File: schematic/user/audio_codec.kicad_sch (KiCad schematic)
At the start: 27 parts, among them U4 TLV320AIC3254IRHBR

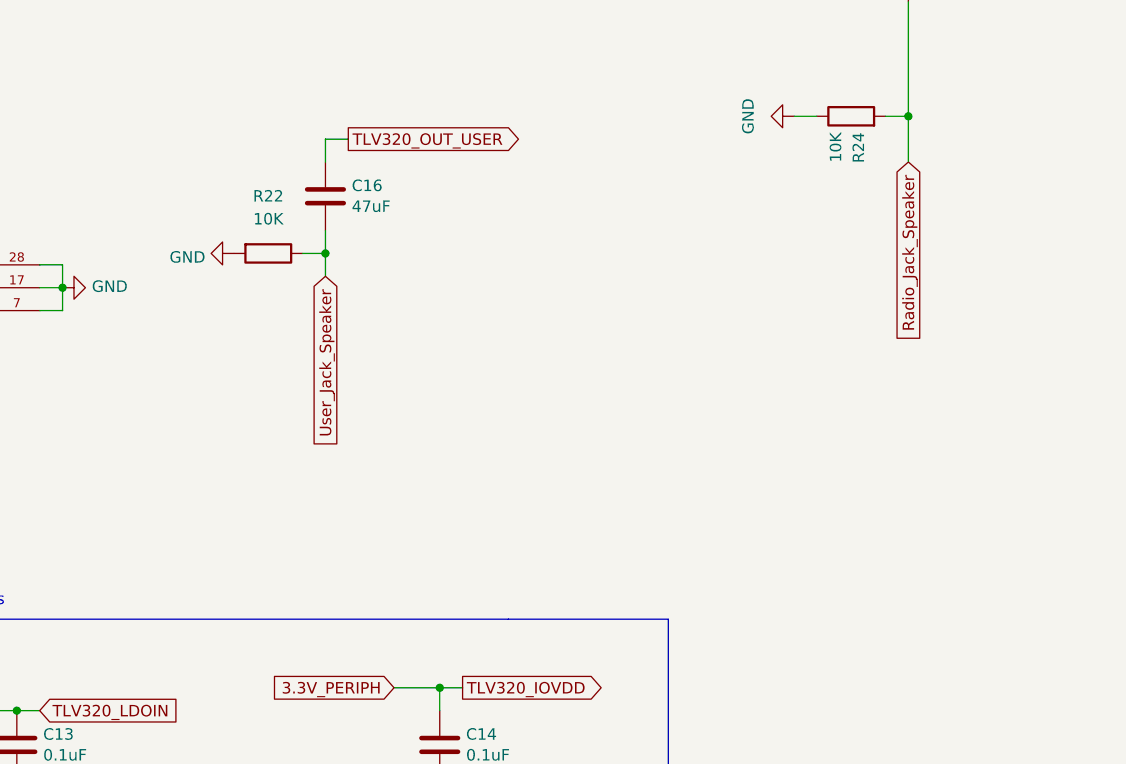
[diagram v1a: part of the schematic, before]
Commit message: v0.7 board: re-add output LPF for audio jacks.
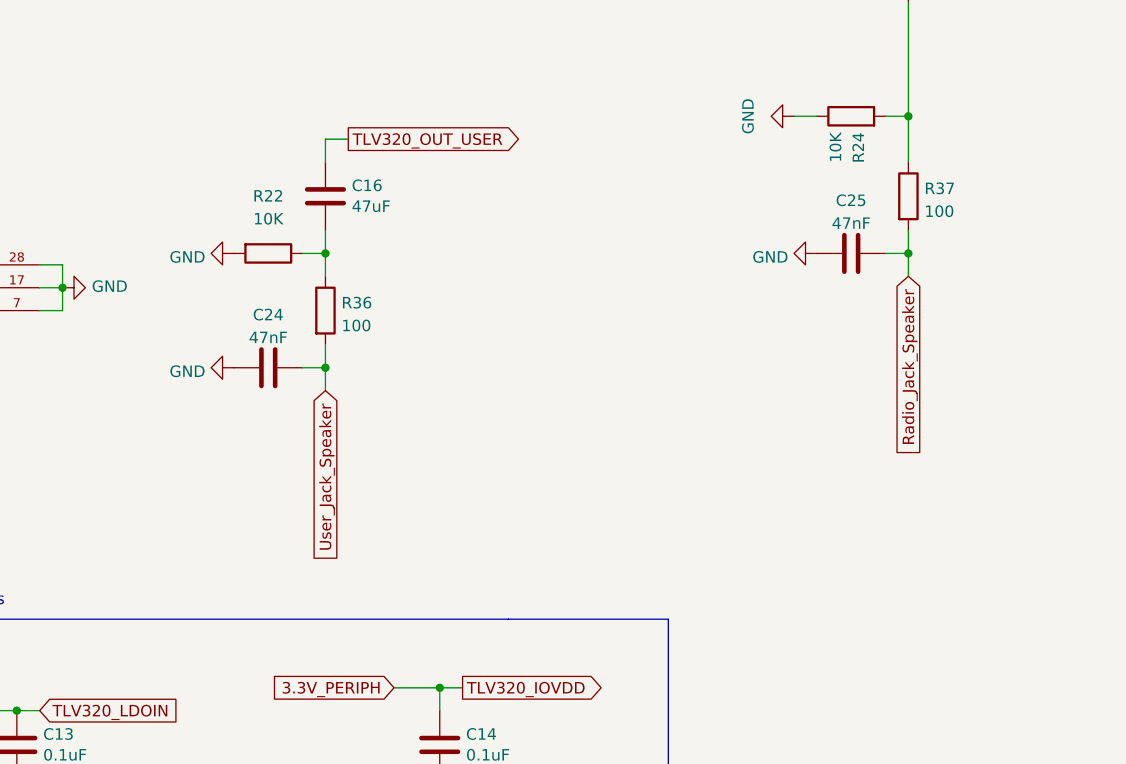
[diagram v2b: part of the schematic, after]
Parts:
- added C24, C25: 47nF, Capacitor_SMD:C_0402_1005Metric, symbol Device:C
- added R36, R37: 100, Resistor_SMD:R_0402_1005Metric, symbol Device:R
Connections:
- net GND: now also C24.1, C25.1
- net Radio_Jack_Speaker: now also C25.2, R37.2; no longer C17.2, R24.2
- net User_Jack_Speaker: now also C24.2, R36.2; no longer C16.2, R22.1
- new net: C16.2, R22.1, R36.1
- new net: C17.2, R24.2, R37.1
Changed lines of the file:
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@@
   (junction (at 39.37 177.8) (diameter 0) (color 0 0 0 0)
   )
+  (junction (at 200.66 123.19) (diameter 0) (color 0 0 0 0)
+  )
   (junction (at 200.66 107.95) (diameter 0) (color 0 0 0 0)
   )
@@
   )
   (junction (at 255.27 27.94) (diameter 0) (color 0 0 0 0)
+  )
+  (junction (at 135.89 135.89) (diameter 0) (color 0 0 0 0)
   )
   (junction (at 106.68 127) (diameter 0) (color 0 0 0 0)
@@
     (stroke (width 0) (type default) (color 0 0 0 0))
   )
+  (wire (pts (xy 200.66 123.19) (xy 200.66 125.73))
+    (stroke (width 0) (type default) (color 0 0 0 0))
+  )
   (wire (pts (xy 106.68 129.54) (xy 106.68 127))
     (stroke (width 0) (type default) (color 0 0 0 0))
@@
     (stroke (width 0) (type default) (color 0 0 0 0))
   )
+  (wire (pts (xy 198.12 123.19) (xy 200.66 123.19))
+    (stroke (width 0) (type default) (color 0 0 0 0))
+  )
   (wire (pts (xy 53.34 83.82) (xy 49.53 83.82))
     (stroke (width 0) (type default) (color 0 0 0 0))
@@
     (stroke (width 0) (type default) (color 0 0 0 0))
   )
+  (wire (pts (xy 133.35 135.89) (xy 135.89 135.89))
+    (stroke (width 0) (type default) (color 0 0 0 0))
+  )
   (wire (pts (xy 40.64 177.8) (xy 39.37 177.8))
     (stroke (width 0) (type default) (color 0 0 0 0))
@@
     (stroke (width 0) (type default) (color 0 0 0 0))
   )
+  (wire (pts (xy 200.66 120.65) (xy 200.66 123.19))
+    (stroke (width 0) (type default) (color 0 0 0 0))
+  )
   (wire (pts (xy 160.02 68.58) (xy 161.29 68.58))
     (stroke (width 0) (type default) (color 0 0 0 0))
@@
     (stroke (width 0) (type default) (color 0 0 0 0))
   )
+  (wire (pts (xy 135.89 135.89) (xy 135.89 133.35))
+    (stroke (width 0) (type default) (color 0 0 0 0))
+  )
   (wire (pts (xy 53.34 88.9) (xy 49.53 88.9))
     (stroke (width 0) (type default) (color 0 0 0 0))
@@
   )
   (wire (pts (xy 53.34 104.14) (xy 50.8 104.14))
+    (stroke (width 0) (type default) (color 0 0 0 0))
+  )
+  (wire (pts (xy 135.89 135.89) (xy 135.89 138.43))
     (stroke (width 0) (type default) (color 0 0 0 0))
   )
@@
     )
   )
-  (global_label "Radio_Jack_Speaker" (shape input) (at 200.66 113.03 270) (fields_autoplaced)
-    (effects (font (size 1.27 1.27)) (justify right))
-    (property "Intersheet References" "${INTERSHEET_REFS}" (id 0) (at 234.95 -99.06 0)
+  (global_label "Radio_Jack_Speaker" (shape input) (at 200.66 125.73 270) (fields_autoplaced)
+    (effects (font (size 1.27 1.27)) (justify right))
+    (property "Intersheet References" "${INTERSHEET_REFS}" (id 0) (at 234.95 -86.36 0)
       (effects (font (size 1.27 1.27)) hide)
     )
@@
     )
   )
-  (global_label "User_Jack_Speaker" (shape input) (at 135.89 125.73 270) (fields_autoplaced)
-    (effects (font (size 1.27 1.27)) (justify right))
-    (property "Intersheet References" "${INTERSHEET_REFS}" (id 0) (at 170.18 -53.34 0)
+  (global_label "User_Jack_Speaker" (shape input) (at 135.89 138.43 270) (fields_autoplaced)
+    (effects (font (size 1.27 1.27)) (justify right))
+    (property "Intersheet References" "${INTERSHEET_REFS}" (id 0) (at 170.18 -40.64 0)
       (effects (font (size 1.27 1.27)) hide)
     )
@@
     (pin "2")
   )
+  (symbol (lib_id "Device:R") (at 200.66 116.84 0) (unit 1)
+    (in_bom yes) (on_board yes) (fields_autoplaced)
+    (property "Reference" "R37" (id 0) (at 202.438 116.0053 0)
+      (effects (font (size 1.27 1.27)) (justify left))
+    )
+    (property "Value" "100" (id 1) (at 202.438 118.5422 0)
+      (effects (font (size 1.27 1.27)) (justify left))
+    )
+    (property "Footprint" "Resistor_SMD:R_0402_1005Metric" (id 2) (at 198.882 116.84 90)
+      (effects (font (size 1.27 1.27)) hide)
+    )
+    (property "Datasheet" "https://datasheet.lcsc.com/lcsc/2205311900_UNI-ROYAL-Uniroyal-Elec-0402WGF1000TCE_C25076.pdf" (id 3) (at 200.66 116.84 0)
+      (effects (font (size 1.27 1.27)) hide)
+    )
+    (property "LCSC" "C25076" (id 4) (at 200.66 116.84 0)
+      (effects (font (size 1.27 1.27)) hide)
+    )
+    (pin "1")
+    (pin "2")
+  )
   (symbol (lib_id "power:GND") (at 148.59 184.15 0) (unit 1)
     (in_bom yes) (on_board yes)
@@
     )
     (property "LCSC" "C47339" (id 4) (at 255.27 34.29 0)
+      (effects (font (size 1.27 1.27)) hide)
+    )
+    (pin "1")
+    (pin "2")
+  )
+  (symbol (lib_id "Device:C") (at 194.31 123.19 90) (unit 1)
+    (in_bom yes) (on_board yes) (fields_autoplaced)
+    (property "Reference" "C25" (id 0) (at 194.31 117.3312 90))
+    (property "Value" "47nF" (id 1) (at 194.31 119.8681 90))
+    (property "Footprint" "Capacitor_SMD:C_0402_1005Metric" (id 2) (at 198.12 122.2248 0)
+      (effects (font (size 1.27 1.27)) hide)
+    )
+    (property "Datasheet" "https://datasheet.lcsc.com/lcsc/2007131538_Murata-Electronics-GCM155R71H473KE02J_C697422.pdf" (id 3) (at 194.31 123.19 0)
+      (effects (font (size 1.27 1.27)) hide)
+    )
+    (property "LCSC" "C697422" (id 4) (at 194.31 123.19 90)
       (effects (font (size 1.27 1.27)) hide)
     )
@@
     (pin "2")
   )
+  (symbol (lib_id "power:GND") (at 125.73 135.89 270) (unit 1)
+    (in_bom yes) (on_board yes) (fields_autoplaced)
+    (property "Reference" "#PWR052" (id 0) (at 119.38 135.89 0)
+      (effects (font (size 1.27 1.27)) hide)
+    )
+    (property "Value" "GND" (id 1) (at 122.5551 136.3238 90)
+      (effects (font (size 1.27 1.27)) (justify right))
+    )
+    (property "Footprint" "" (id 2) (at 125.73 135.89 0)
+      (effects (font (size 1.27 1.27)) hide)
+    )
+    (property "Datasheet" "" (id 3) (at 125.73 135.89 0)
+      (effects (font (size 1.27 1.27)) hide)
+    )
+    (pin "1")
+  )
   (symbol (lib_id "power:GND") (at 91.44 184.15 0) (unit 1)
     (in_bom yes) (on_board yes)
@@
     (pin "2")
   )
+  (symbol (lib_id "Device:C") (at 129.54 135.89 90) (unit 1)
+    (in_bom yes) (on_board yes) (fields_autoplaced)
+    (property "Reference" "C24" (id 0) (at 129.54 130.0312 90))
+    (property "Value" "47nF" (id 1) (at 129.54 132.5681 90))
+    (property "Footprint" "Capacitor_SMD:C_0402_1005Metric" (id 2) (at 133.35 134.9248 0)
+      (effects (font (size 1.27 1.27)) hide)
+    )
+    (property "Datasheet" "https://datasheet.lcsc.com/lcsc/2007131538_Murata-Electronics-GCM155R71H473KE02J_C697422.pdf" (id 3) (at 129.54 135.89 0)
+      (effects (font (size 1.27 1.27)) hide)
+    )
+    (property "LCSC" "C697422" (id 4) (at 129.54 135.89 90)
+      (effects (font (size 1.27 1.27)) hide)
+    )
+    (pin "1")
+    (pin "2")
+  )
   (symbol (lib_id "power:GND") (at 50.8 114.3 270) (unit 1)
     (in_bom yes) (on_board yes)
@@
     (pin "2")
   )
+  (symbol (lib_id "power:GND") (at 190.5 123.19 270) (unit 1)
+    (in_bom yes) (on_board yes) (fields_autoplaced)
+    (property "Reference" "#PWR053" (id 0) (at 184.15 123.19 0)
+      (effects (font (size 1.27 1.27)) hide)
+    )
+    (property "Value" "GND" (id 1) (at 187.3251 123.6238 90)
+      (effects (font (size 1.27 1.27)) (justify right))
+    )
+    (property "Footprint" "" (id 2) (at 190.5 123.19 0)
+      (effects (font (size 1.27 1.27)) hide)
+    )
+    (property "Datasheet" "" (id 3) (at 190.5 123.19 0)
+      (effects (font (size 1.27 1.27)) hide)
+    )
+    (pin "1")
+  )
   (symbol (lib_id "Device:R") (at 255.27 123.19 270) (unit 1)
     (in_bom yes) (on_board yes)
@@
     (pin "1")
   )
+  (symbol (lib_id "Device:R") (at 135.89 129.54 0) (unit 1)
+    (in_bom yes) (on_board yes) (fields_autoplaced)
+    (property "Reference" "R36" (id 0) (at 137.668 128.7053 0)
+      (effects (font (size 1.27 1.27)) (justify left))
+    )
+    (property "Value" "100" (id 1) (at 137.668 131.2422 0)
+      (effects (font (size 1.27 1.27)) (justify left))
+    )
+    (property "Footprint" "Resistor_SMD:R_0402_1005Metric" (id 2) (at 134.112 129.54 90)
+      (effects (font (size 1.27 1.27)) hide)
+    )
+    (property "Datasheet" "https://datasheet.lcsc.com/lcsc/2205311900_UNI-ROYAL-Uniroyal-Elec-0402WGF1000TCE_C25076.pdf" (id 3) (at 135.89 129.54 0)
+      (effects (font (size 1.27 1.27)) hide)
+    )
+    (property "LCSC" "C25076" (id 4) (at 135.89 129.54 0)
+      (effects (font (size 1.27 1.27)) hide)
+    )
+    (pin "1")
+    (pin "2")
+  )
 )

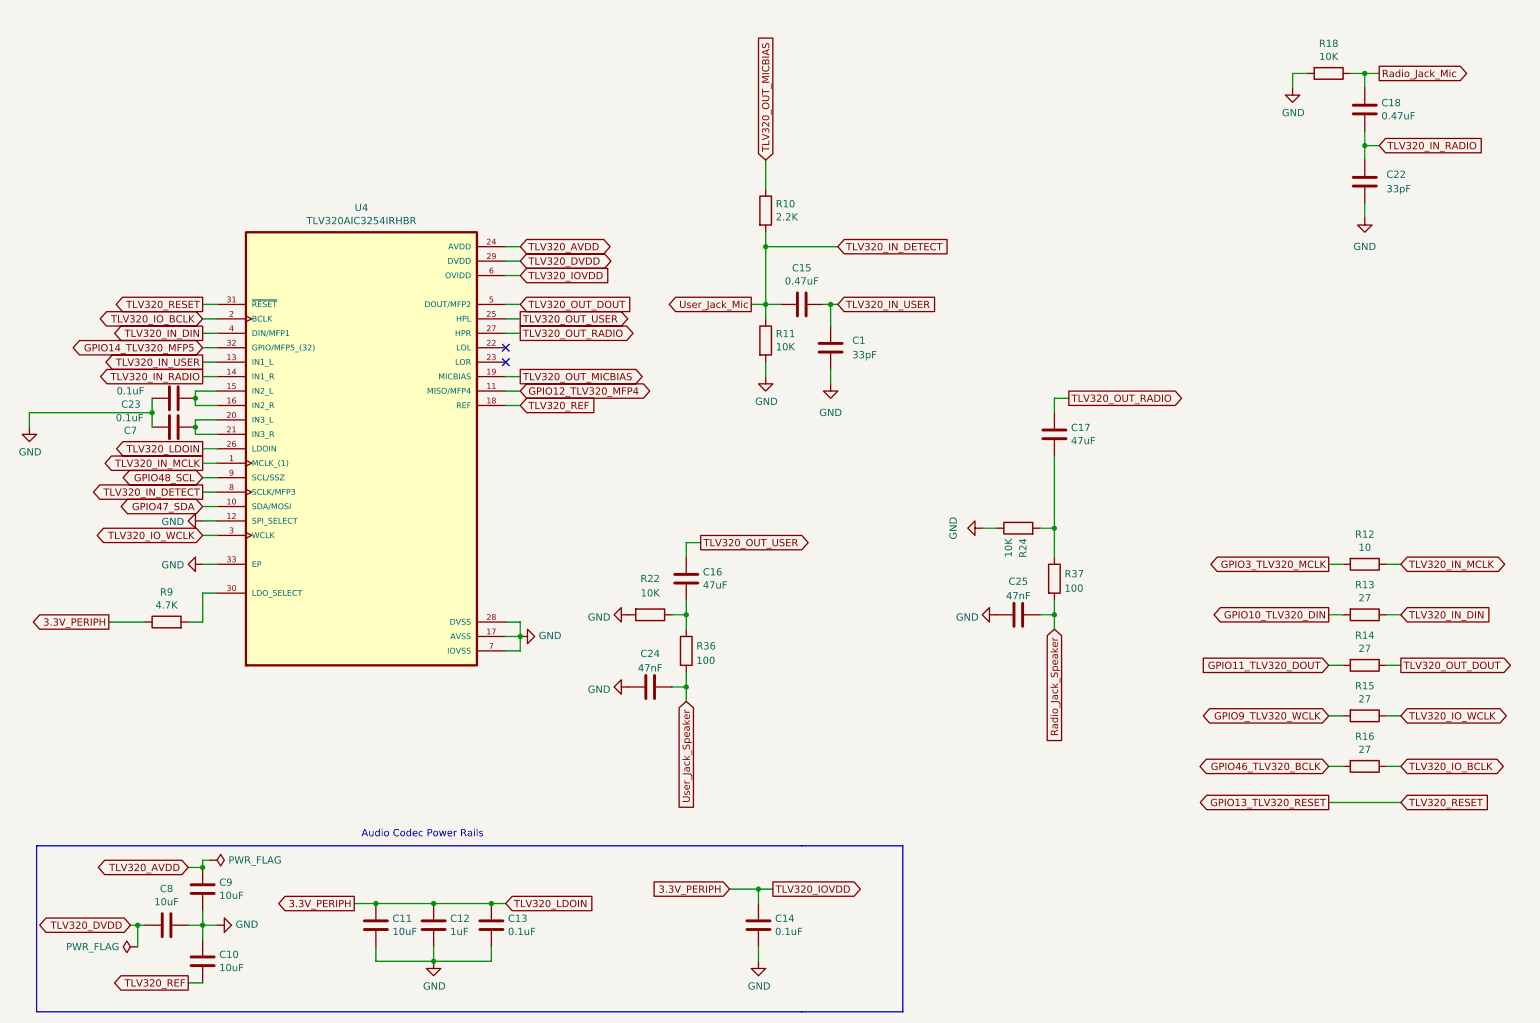
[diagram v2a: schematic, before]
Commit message: v0.7 board: clarify/improve cap ratings to account for TVS diode clamp voltage.
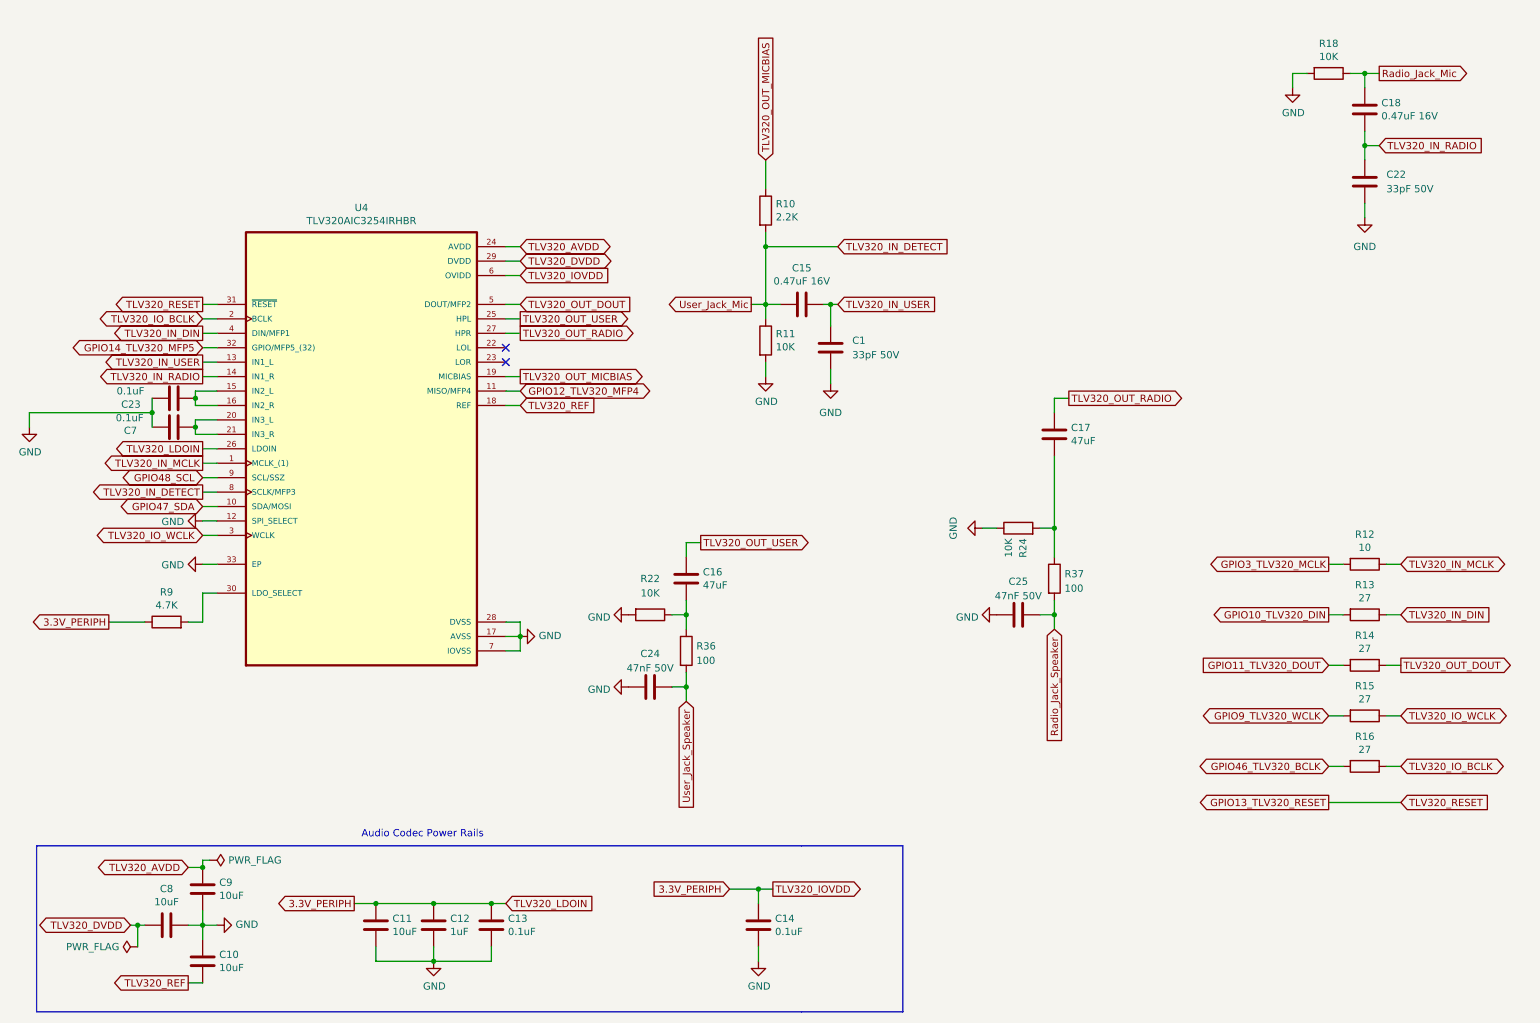
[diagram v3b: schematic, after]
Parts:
- C1, C22: value 33pF -> 33pF 50V
- C15, C18: value 0.47uF -> 0.47uF 16V; LCSC C47339 -> C575468
- C24, C25: value 47nF -> 47nF 50V
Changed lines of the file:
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@@
     (in_bom yes) (on_board yes)
     (property "Reference" "C15" (id 0) (at 156.21 62.1792 90))
-    (property "Value" "0.47uF" (id 1) (at 156.21 64.4906 90))
+    (property "Value" "0.47uF 16V" (id 1) (at 156.21 64.4906 90))
     (property "Footprint" "Capacitor_SMD:C_0402_1005Metric" (id 2) (at 160.02 67.6148 0)
       (effects (font (size 1.27 1.27)) hide)
     )
-    (property "Datasheet" "https://datasheet.lcsc.com/lcsc/1810191214_Samsung-Electro-Mechanics-CL05A474KP5NNNC-_C47339.pdf" (id 3) (at 156.21 68.58 0)
-      (effects (font (size 1.27 1.27)) hide)
-    )
-    (property "LCSC" "C47339" (id 4) (at 156.21 68.58 0)
+    (property "Datasheet" "https://datasheet.lcsc.com/lcsc/2006031032_Walsin-Tech-Corp-0402X474K160CT_C575468.pdf" (id 3) (at 156.21 68.58 0)
+      (effects (font (size 1.27 1.27)) hide)
+    )
+    (property "LCSC" "C575468" (id 4) (at 156.21 68.58 0)
       (effects (font (size 1.27 1.27)) hide)
     )
@@
       (effects (font (size 1.27 1.27)) (justify left))
     )
-    (property "Value" "33pF" (id 1) (at 165.1 77.4699 0)
+    (property "Value" "33pF 50V" (id 1) (at 165.1 77.4699 0)
       (effects (font (size 1.27 1.27)) (justify left))
     )
@@
       (effects (font (size 1.27 1.27)) (justify left))
     )
-    (property "Value" "0.47uF" (id 1) (at 258.191 35.433 0)
+    (property "Value" "0.47uF 16V" (id 1) (at 258.191 35.433 0)
       (effects (font (size 1.27 1.27)) (justify left))
     )
@@
       (effects (font (size 1.27 1.27)) hide)
     )
-    (property "Datasheet" "https://datasheet.lcsc.com/lcsc/1810191214_Samsung-Electro-Mechanics-CL05A474KP5NNNC-_C47339.pdf" (id 3) (at 255.27 34.29 0)
-      (effects (font (size 1.27 1.27)) hide)
-    )
-    (property "LCSC" "C47339" (id 4) (at 255.27 34.29 0)
+    (property "Datasheet" "https://datasheet.lcsc.com/lcsc/2006031032_Walsin-Tech-Corp-0402X474K160CT_C575468.pdf" (id 3) (at 255.27 34.29 0)
+      (effects (font (size 1.27 1.27)) hide)
+    )
+    (property "LCSC" "C575468" (id 4) (at 255.27 34.29 0)
       (effects (font (size 1.27 1.27)) hide)
     )
@@
     (in_bom yes) (on_board yes) (fields_autoplaced)
     (property "Reference" "C25" (id 0) (at 194.31 117.3312 90))
-    (property "Value" "47nF" (id 1) (at 194.31 119.8681 90))
+    (property "Value" "47nF 50V" (id 1) (at 194.31 119.8681 90))
     (property "Footprint" "Capacitor_SMD:C_0402_1005Metric" (id 2) (at 198.12 122.2248 0)
       (effects (font (size 1.27 1.27)) hide)
@@
       (effects (font (size 1.27 1.27)) (justify left))
     )
-    (property "Value" "33pF" (id 1) (at 259.08 48.2599 0)
+    (property "Value" "33pF 50V" (id 1) (at 259.08 48.2599 0)
       (effects (font (size 1.27 1.27)) (justify left))
     )
@@
     (in_bom yes) (on_board yes) (fields_autoplaced)
     (property "Reference" "C24" (id 0) (at 129.54 130.0312 90))
-    (property "Value" "47nF" (id 1) (at 129.54 132.5681 90))
+    (property "Value" "47nF 50V" (id 1) (at 129.54 132.5681 90))
     (property "Footprint" "Capacitor_SMD:C_0402_1005Metric" (id 2) (at 133.35 134.9248 0)
       (effects (font (size 1.27 1.27)) hide)
